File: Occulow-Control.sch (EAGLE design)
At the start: 11 parts, among them T1 DMP3010LK3

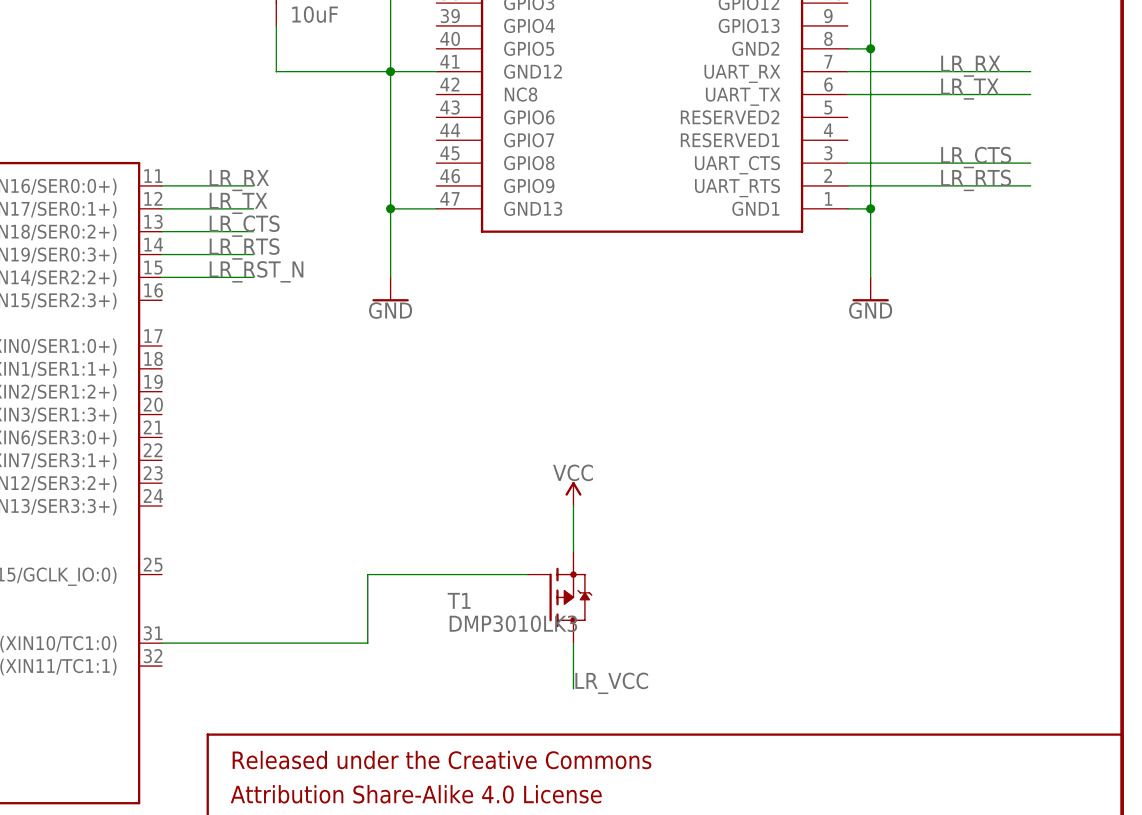
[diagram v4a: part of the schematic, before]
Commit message: Moved lora off i2c pins, grideye header
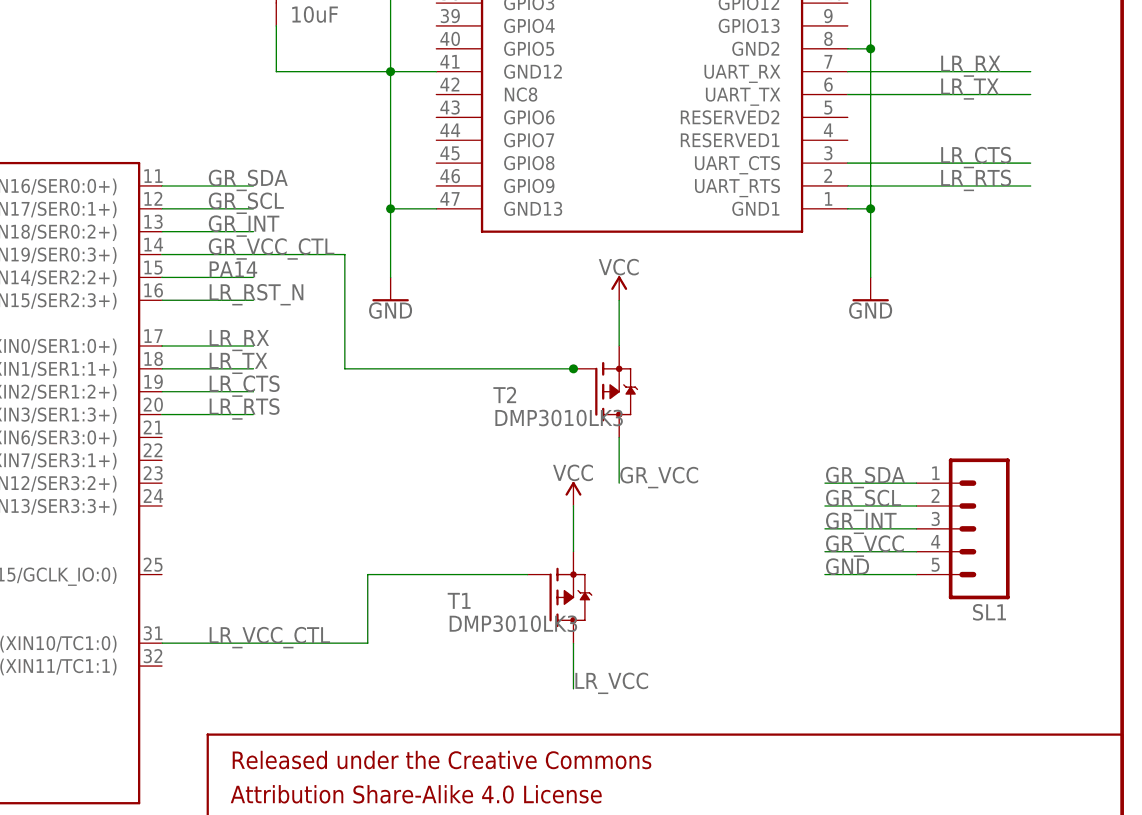
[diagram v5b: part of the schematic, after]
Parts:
- added SL1: (no value), con-amp-quick:M05
- added T2: DMP3010LK3, transistor-fet:SPD30P06PTO252
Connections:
- net N$2 renamed LR_VCC_CTL
- new net GR_INT: SL1.3, U$1.PA10(AIN18/SER0:2+)
- new net GR_SCL: SL1.2, U$1.PA09(I2C/AIN17/SER0:1+)
- new net GR_SDA: SL1.1, U$1.PA08(I2C/NMI/AIN16/SER0:0+)
- new net GR_VCC: SL1.4, T2.D
- new net GR_VCC_CTL: T2.G, U$1.PA11(AIN19/SER0:3+)
- new net PA14: U$1.PA14(XIN14/SER2:2+)
- net GND: now also SL1.5
- net LR_CTS: now also U$1.PA18(XIN2/SER1:2+); no longer U$1.PA10(AIN18/SER0:2+)
- net LR_RST_N: now also U$1.PA15(XIN15/SER2:3+); no longer U$1.PA14(XIN14/SER2:2+)
- net LR_RTS: now also U$1.PA19(XIN3/SER1:3+); no longer U$1.PA11(AIN19/SER0:3+)
- net LR_RX: now also U$1.PA16(I2C/XIN0/SER1:0+); no longer U$1.PA08(I2C/NMI/AIN16/SER0:0+)
- net LR_TX: now also U$1.PA17(I2C/XIN1/SER1:1+); no longer U$1.PA09(I2C/AIN17/SER0:1+)
- net VCC: now also T2.S
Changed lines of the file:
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@@
 <part name="T1" library="transistor-fet" deviceset="SPD30P06P" device="TO252" value="DMP3010LK3"/>
 <part name="SUPPLY2" library="SparkFun-PowerSymbols" deviceset="VCC" device=""/>
+<part name="SL1" library="con-amp-quick" deviceset="M05" device=""/>
+<part name="T2" library="transistor-fet" deviceset="SPD30P06P" device="TO252" value="DMP3010LK3"/>
+<part name="SUPPLY3" library="SparkFun-PowerSymbols" deviceset="VCC" device=""/>
 </parts>
 <sheets>
@@
 <instance part="T1" gate="G$1" x="185.42" y="50.8"/>
 <instance part="SUPPLY2" gate="G$1" x="187.96" y="60.96"/>
+<instance part="SL1" gate="G$1" x="233.68" y="58.42" rot="R180"/>
+<instance part="T2" gate="G$1" x="190.5" y="73.66"/>
+<instance part="SUPPLY3" gate="G$1" x="193.04" y="83.82"/>
 </instances>
 <busses>
@@
 <pinref part="GND8" gate="1" pin="GND"/>
 </segment>
+<segment>
+<pinref part="SL1" gate="G$1" pin="5"/>
+<wire x1="226.06" y1="53.34" x2="215.9" y2="53.34" width="0.1524" layer="91"/>
+<label x="215.9" y="53.34" size="1.778" layer="95"/>
+</segment>
 </net>
 <net name="VCC" class="0">
@@
 <wire x1="187.96" y1="60.96" x2="187.96" y2="55.88" width="0.1524" layer="91"/>
 </segment>
+<segment>
+<pinref part="SUPPLY3" gate="G$1" pin="VCC"/>
+<pinref part="T2" gate="G$1" pin="S"/>
+<wire x1="193.04" y1="83.82" x2="193.04" y2="78.74" width="0.1524" layer="91"/>
+</segment>
 </net>
 <net name="N$1" class="0">
@@
 </segment>
 <segment>
-<pinref part="U$1" gate="G$1" pin="PA08(I2C/NMI/AIN16/SER0:0+)"/>
-<wire x1="142.24" y1="96.52" x2="152.4" y2="96.52" width="0.1524" layer="91"/>
-<label x="147.32" y="96.52" size="1.778" layer="95"/>
+<pinref part="U$1" gate="G$1" pin="PA16(I2C/XIN0/SER1:0+)"/>
+<wire x1="142.24" y1="78.74" x2="152.4" y2="78.74" width="0.1524" layer="91"/>
+<label x="147.32" y="78.74" size="1.778" layer="95"/>
 </segment>
 </net>
@@
 </segment>
 <segment>
-<pinref part="U$1" gate="G$1" pin="PA09(I2C/AIN17/SER0:1+)"/>
-<wire x1="142.24" y1="93.98" x2="152.4" y2="93.98" width="0.1524" layer="91"/>
-<label x="147.32" y="93.98" size="1.778" layer="95"/>
+<pinref part="U$1" gate="G$1" pin="PA17(I2C/XIN1/SER1:1+)"/>
+<wire x1="142.24" y1="76.2" x2="152.4" y2="76.2" width="0.1524" layer="91"/>
+<label x="147.32" y="76.2" size="1.778" layer="95"/>
 </segment>
 </net>
@@
 </segment>
 <segment>
-<pinref part="U$1" gate="G$1" pin="PA10(AIN18/SER0:2+)"/>
-<wire x1="142.24" y1="91.44" x2="152.4" y2="91.44" width="0.1524" layer="91"/>
-<label x="147.32" y="91.44" size="1.778" layer="95"/>
+<pinref part="U$1" gate="G$1" pin="PA18(XIN2/SER1:2+)"/>
+<wire x1="142.24" y1="73.66" x2="152.4" y2="73.66" width="0.1524" layer="91"/>
+<label x="147.32" y="73.66" size="1.778" layer="95"/>
 </segment>
 </net>
@@
 </segment>
 <segment>
-<pinref part="U$1" gate="G$1" pin="PA11(AIN19/SER0:3+)"/>
-<wire x1="142.24" y1="88.9" x2="152.4" y2="88.9" width="0.1524" layer="91"/>
-<label x="147.32" y="88.9" size="1.778" layer="95"/>
+<pinref part="U$1" gate="G$1" pin="PA19(XIN3/SER1:3+)"/>
+<wire x1="142.24" y1="71.12" x2="152.4" y2="71.12" width="0.1524" layer="91"/>
+<label x="147.32" y="71.12" size="1.778" layer="95"/>
 </segment>
 </net>
@@
 </segment>
 <segment>
-<pinref part="U$1" gate="G$1" pin="PA14(XIN14/SER2:2+)"/>
-<wire x1="142.24" y1="86.36" x2="152.4" y2="86.36" width="0.1524" layer="91"/>
-<label x="147.32" y="86.36" size="1.778" layer="95"/>
-</segment>
-</net>
-<net name="N$2" class="0">
+<pinref part="U$1" gate="G$1" pin="PA15(XIN15/SER2:3+)"/>
+<wire x1="142.24" y1="83.82" x2="152.4" y2="83.82" width="0.1524" layer="91"/>
+<label x="147.32" y="83.82" size="1.778" layer="95"/>
+</segment>
+</net>
+<net name="LR_VCC_CTL" class="0">
 <segment>
 <pinref part="U$1" gate="G$1" pin="PA30(XIN10/TC1:0)"/>
@@
 <pinref part="T1" gate="G$1" pin="G"/>
 <wire x1="165.1" y1="53.34" x2="182.88" y2="53.34" width="0.1524" layer="91"/>
-</segment>
-</net>
+<label x="147.32" y="45.72" size="1.778" layer="95"/>
+</segment>
+</net>
+<net name="GR_SDA" class="0">
+<segment>
+<pinref part="U$1" gate="G$1" pin="PA08(I2C/NMI/AIN16/SER0:0+)"/>
+<wire x1="142.24" y1="96.52" x2="152.4" y2="96.52" width="0.1524" layer="91"/>
+<label x="147.32" y="96.52" size="1.778" layer="95"/>
+</segment>
+<segment>
+<pinref part="SL1" gate="G$1" pin="1"/>
+<wire x1="226.06" y1="63.5" x2="215.9" y2="63.5" width="0.1524" layer="91"/>
+<label x="215.9" y="63.5" size="1.778" layer="95"/>
+</segment>
+</net>
+<net name="GR_SCL" class="0">
+<segment>
+<pinref part="U$1" gate="G$1" pin="PA09(I2C/AIN17/SER0:1+)"/>
+<wire x1="142.24" y1="93.98" x2="152.4" y2="93.98" width="0.1524" layer="91"/>
+<label x="147.32" y="93.98" size="1.778" layer="95"/>
+</segment>
+<segment>
+<pinref part="SL1" gate="G$1" pin="2"/>
+<wire x1="226.06" y1="60.96" x2="215.9" y2="60.96" width="0.1524" layer="91"/>
+<label x="215.9" y="60.96" size="1.778" layer="95"/>
+</segment>
+</net>
+<net name="GR_INT" class="0">
+<segment>
+<pinref part="U$1" gate="G$1" pin="PA10(AIN18/SER0:2+)"/>
+<wire x1="142.24" y1="91.44" x2="152.4" y2="91.44" width="0.1524" layer="91"/>
+<label x="147.32" y="91.44" size="1.778" layer="95"/>
+</segment>
+<segment>
+<pinref part="SL1" gate="G$1" pin="3"/>
+<wire x1="226.06" y1="58.42" x2="215.9" y2="58.42" width="0.1524" layer="91"/>
+<label x="215.9" y="58.42" size="1.778" layer="95"/>
+</segment>
+</net>
+<net name="GR_VCC_CTL" class="0">
+<segment>
+<pinref part="U$1" gate="G$1" pin="PA11(AIN19/SER0:3+)"/>
+<label x="147.32" y="88.9" size="1.778" layer="95"/>
+<pinref part="T2" gate="G$1" pin="G"/>
+<junction x="187.96" y="76.2"/>
+<wire x1="187.96" y1="76.2" x2="162.56" y2="76.2" width="0.1524" layer="91"/>
+<wire x1="162.56" y1="76.2" x2="162.56" y2="88.9" width="0.1524" layer="91"/>
+<wire x1="162.56" y1="88.9" x2="142.24" y2="88.9" width="0.1524" layer="91"/>
+</segment>
+</net>
+<net name="PA14" class="0">
+<segment>
+<pinref part="U$1" gate="G$1" pin="PA14(XIN14/SER2:2+)"/>
+<wire x1="142.24" y1="86.36" x2="152.4" y2="86.36" width="0.1524" layer="91"/>
+<label x="147.32" y="86.36" size="1.778" layer="95"/>
+</segment>
+</net>
+<net name="GR_VCC" class="0">
+<segment>
+<pinref part="T2" gate="G$1" pin="D"/>
+<wire x1="193.04" y1="68.58" x2="193.04" y2="63.5" width="0.1524" layer="91"/>
+<label x="193.04" y="63.5" size="1.778" layer="95"/>
+</segment>
+<segment>
+<pinref part="SL1" gate="G$1" pin="4"/>
+<wire x1="226.06" y1="55.88" x2="215.9" y2="55.88" width="0.1524" layer="91"/>
+<label x="215.9" y="55.88" size="1.778" layer="95"/>
+</segment>
+</net>

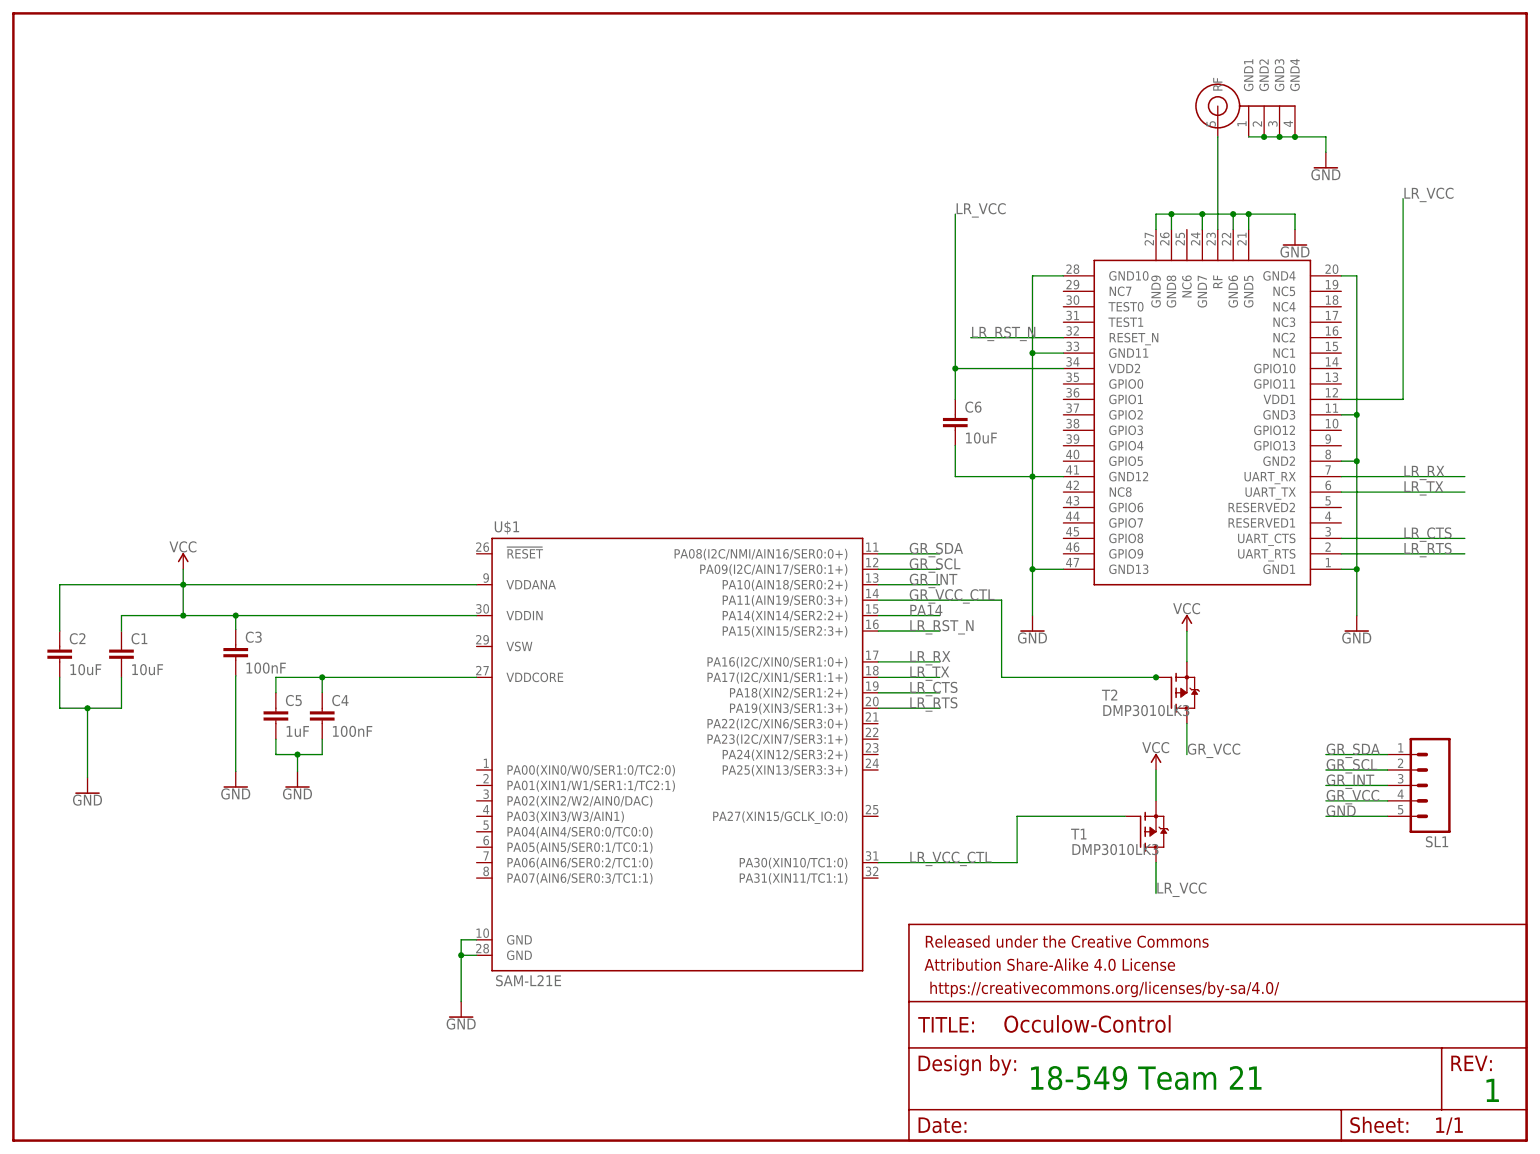
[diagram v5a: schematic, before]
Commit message: PIR control header, unused gpio to header
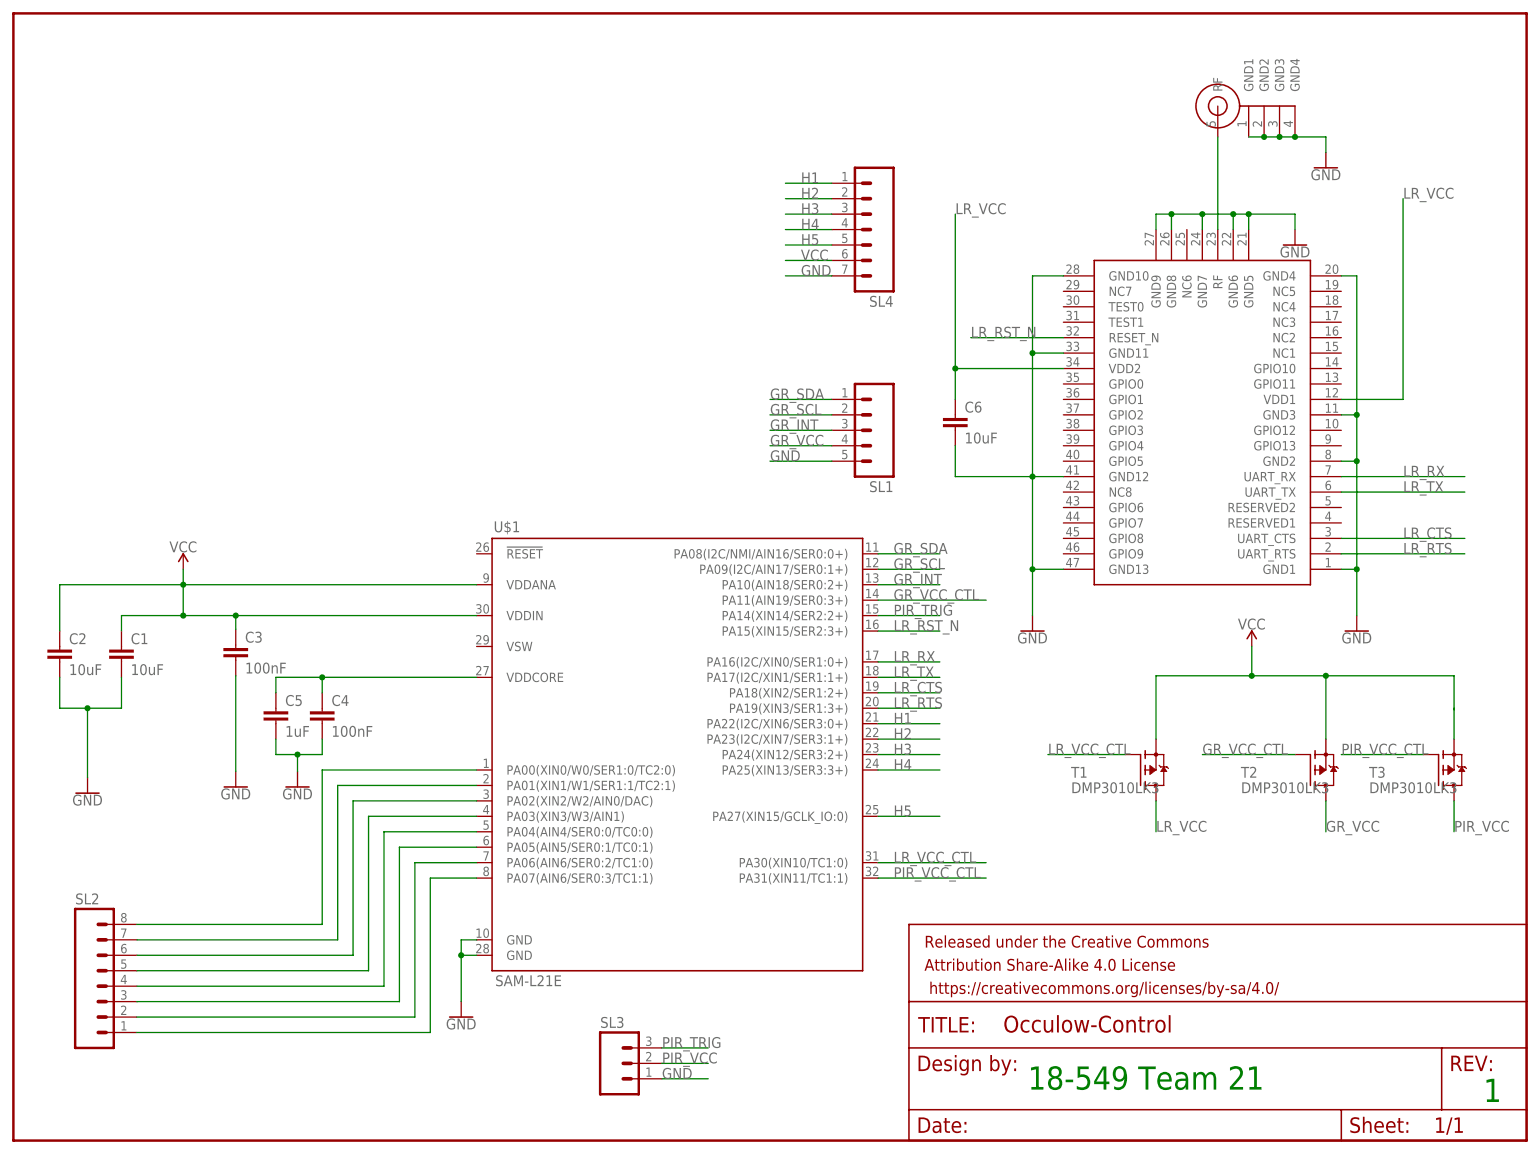
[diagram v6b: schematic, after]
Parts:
- added SL2: (no value), con-amp-quick:M08
- added SL3: (no value), con-amp-quick:M03
- added SL4: (no value), con-amp-quick:M07
- added T3: DMP3010LK3, transistor-fet:SPD30P06PTO252
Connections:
- removed net PA14: U$1.PA14(XIN14/SER2:2+)
- new net H1: SL4.1, U$1.PA22(I2C/XIN6/SER3:0+)
- new net H2: SL4.2, U$1.PA23(I2C/XIN7/SER3:1+)
- new net H3: SL4.3, U$1.PA24(XIN12/SER3:2+)
- new net H4: SL4.4, U$1.PA25(XIN13/SER3:3+)
- new net H5: SL4.5, U$1.PA27(XIN15/GCLK_IO:0)
- new net N$2: SL2.8, U$1.PA00(XIN0/W0/SER1:0/TC2:0)
- new net N$3: SL2.7, U$1.PA01(XIN1/W1/SER1:1/TC2:1)
- new net N$4: SL2.6, U$1.PA02(XIN2/W2/AIN0/DAC)
- new net N$5: SL2.5, U$1.PA03(XIN3/W3/AIN1)
- new net N$6: SL2.4, U$1.PA04(AIN4/SER0:0/TC0:0)
- new net N$7: SL2.3, U$1.PA05(AIN5/SER0:1/TC0:1)
- new net N$8: SL2.2, U$1.PA06(AIN6/SER0:2/TC1:0)
- new net N$9: SL2.1, U$1.PA07(AIN6/SER0:3/TC1:1)
- new net PIR_TRIG: SL3.3, U$1.PA14(XIN14/SER2:2+)
- new net PIR_VCC: SL3.2, T3.D
- new net PIR_VCC_CTL: T3.G, U$1.PA31(XIN11/TC1:1)
- net GND: now also SL3.1, SL4.7
- net VCC: now also SL4.6, T3.S
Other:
- moved on the sheet: SL1, T1, T2
